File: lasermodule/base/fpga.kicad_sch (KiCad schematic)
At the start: 20 parts, among them U12 ICE40UP5K-SG48ITR-FPGA_Lattice, U13 S25FL064LABMFI010, U14 MCP1700x-120xxTT

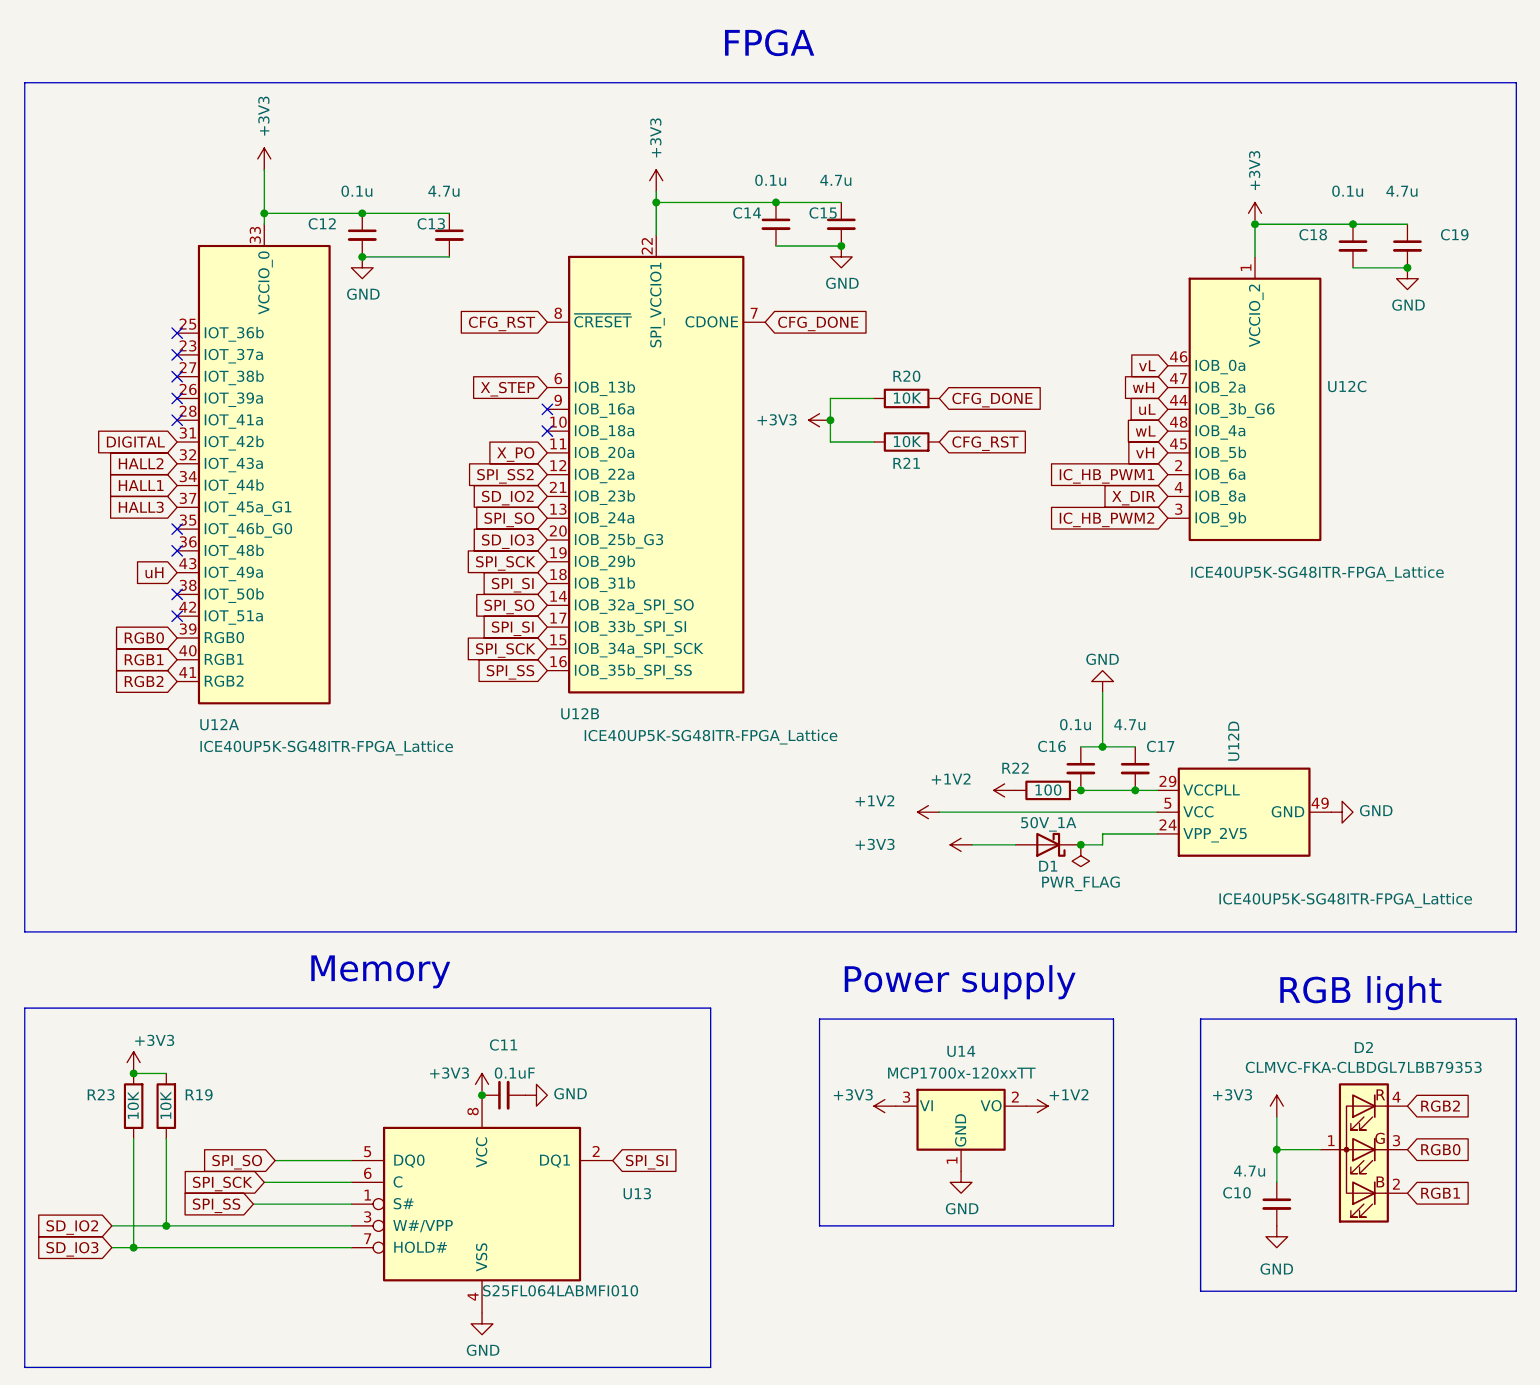
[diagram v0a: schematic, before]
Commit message: added pcbmotor, renamed some folders
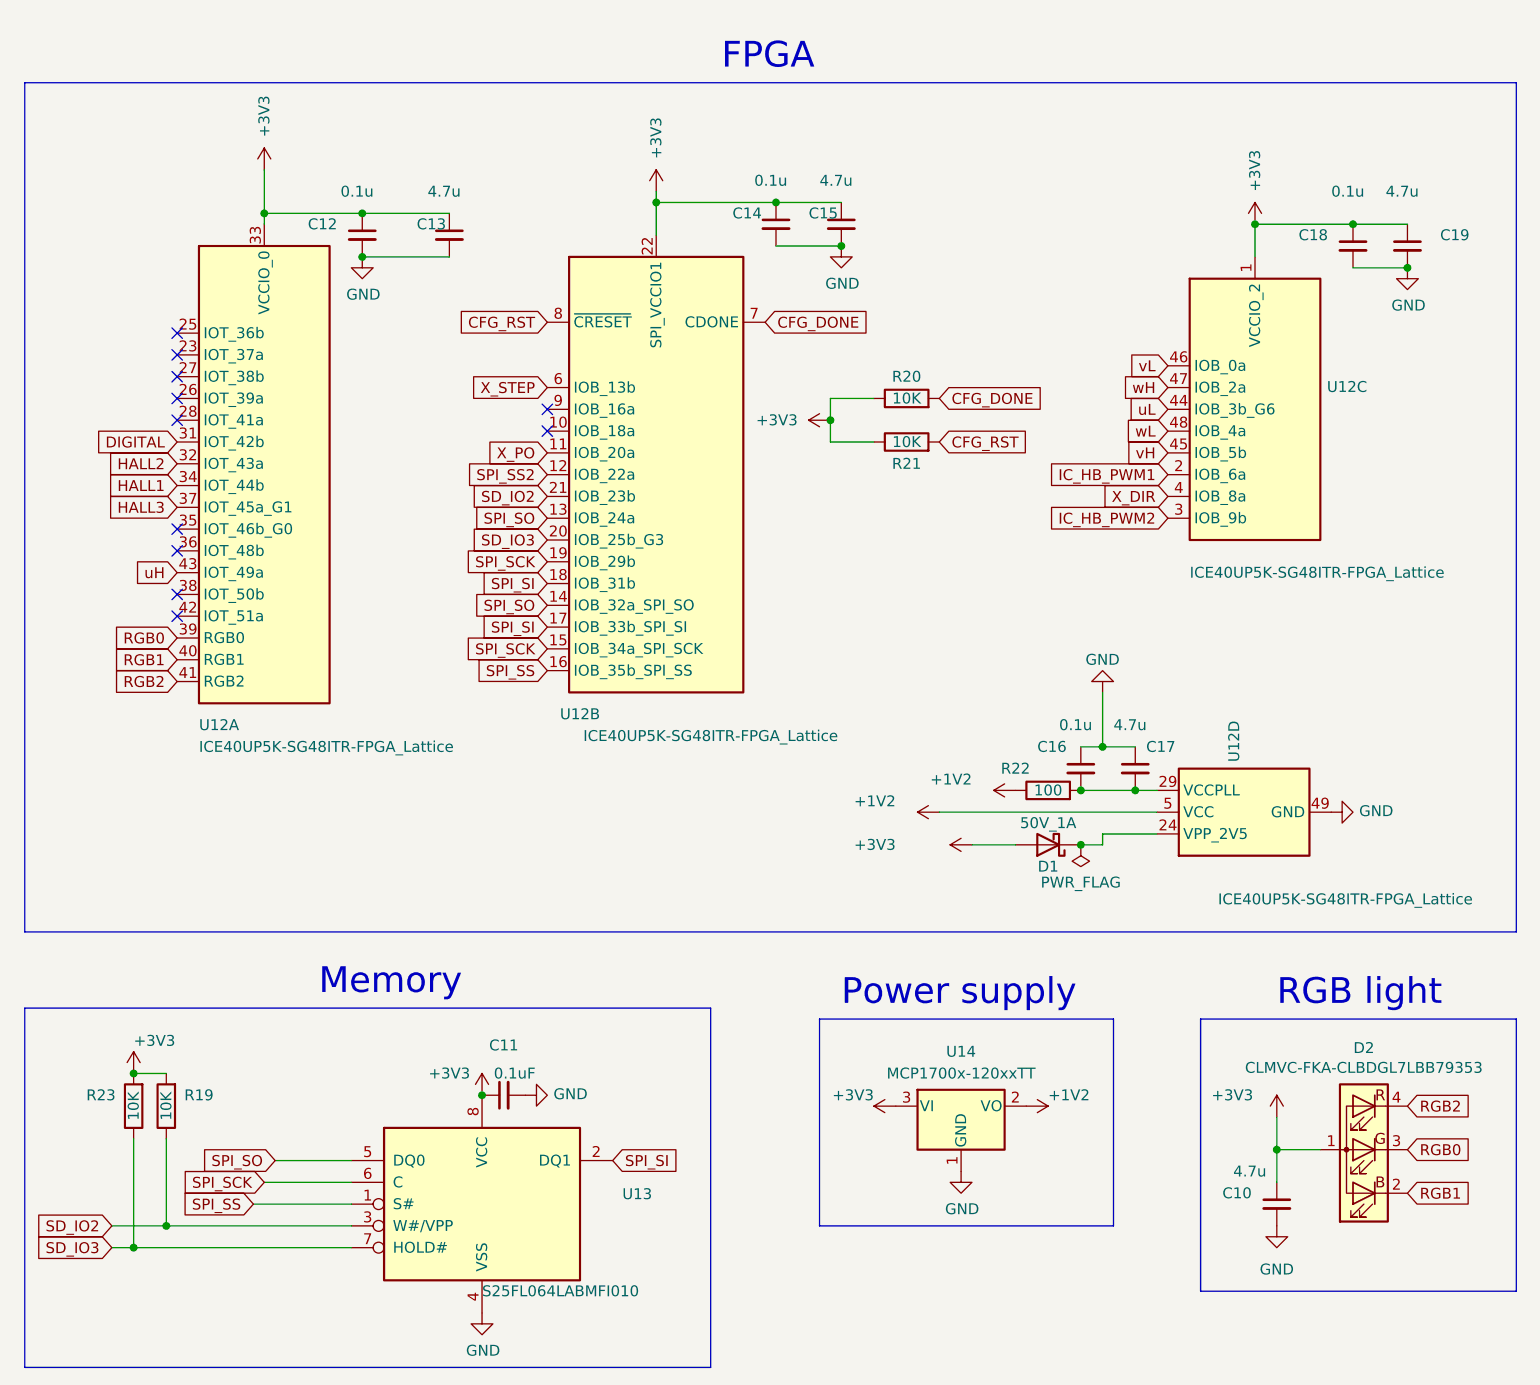
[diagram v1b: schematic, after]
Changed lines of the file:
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@@
     (stroke (width 0) (type default))
   )
-  (text "Power supply" (at 157.48 129.54 0)
+  (text "Power supply" (at 157.48 130.81 0)
     (effects (font (size 3 3)) (justify left bottom))
   )
-  (text "FPGA" (at 143.51 20.32 0)
+  (text "FPGA" (at 143.51 21.59 0)
     (effects (font (size 3 3)) (justify left bottom))
   )
@@
     (effects (font (size 3 3)) (justify left bottom))
   )
-  (text "Memory" (at 95.25 128.27 0)
+  (text "Memory" (at 96.52 129.54 0)
     (effects (font (size 3 3)) (justify left bottom))
   )

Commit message: further cleaned up and tested renders in blender
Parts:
- D2: footprint LED_SMD:LED_Cree-PLCC4_2x2mm_CW -> sockets_scanhead:LED_Cree-PLCC4_2x2mm_CW
- U13: footprint Package_SO:SOIC-8W_5.3x5.3mm_P1.27mm -> sockets_scanhead:SOIC-8W_5.3x5.3mm_P1.27mm
